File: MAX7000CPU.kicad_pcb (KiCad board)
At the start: 2 copper layers, 148.5 x 122 mm, 96 parts, among them J1 JTAG Conn_02x05_Odd_Even, J2 Instructions Conn_01x08_Male, J3 Module Input Conn_01x08_Male, J4 Module Output Conn_01x08_Male, J5 QPI Out Conn_01x08_Male, J6 QPI IN Conn_01x08_Male, J7 Conn_01x05_Male, J8 Barrel_Jack, SW1 Step SW_Push, SW2 CLK Mode SW_Push, SW3 Prog Select SW_DIP_x04, SW4 Reset SW_Push, U1 NE555P, U10 74LS573, U11 74LS241, U12 74LS241, U13 74LS573, U14 74LS573, U15 74LS573, U16 74LS573, U17 EPM7128slc84-15n, U18 LM2596S-5, U19 74LS241, U2 NE555P, U20 74LS241, U3 NE555P, U4 CLVC1GX04MDRLREP, U5 EPM7128slc84-15n, U6 74LS573, U7 SN74HC161N, U8 SN74HC161N, U9 IDT7132, Y1 Crystal

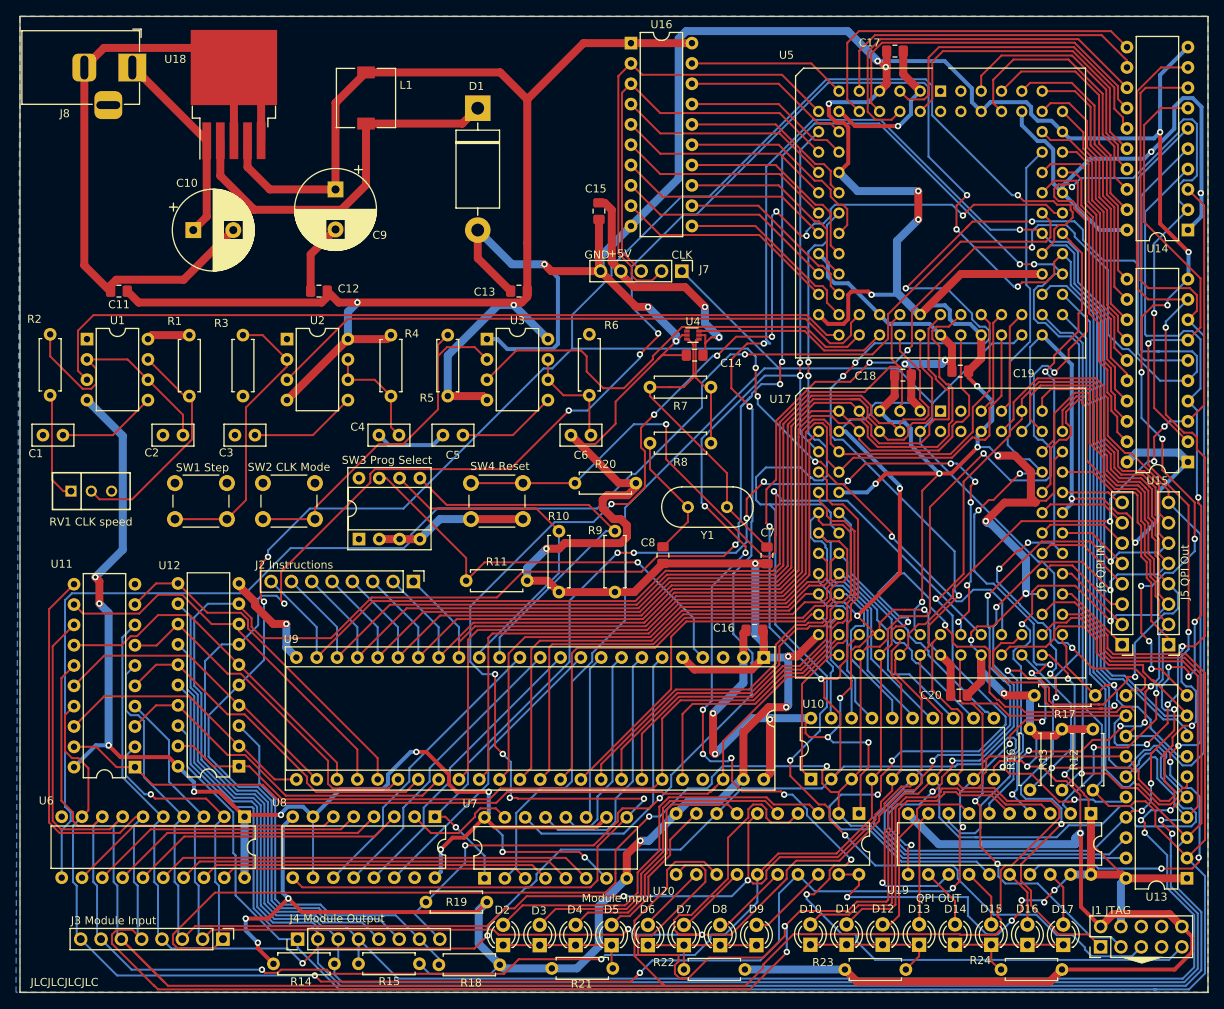
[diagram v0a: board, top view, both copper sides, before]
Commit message: auto routed
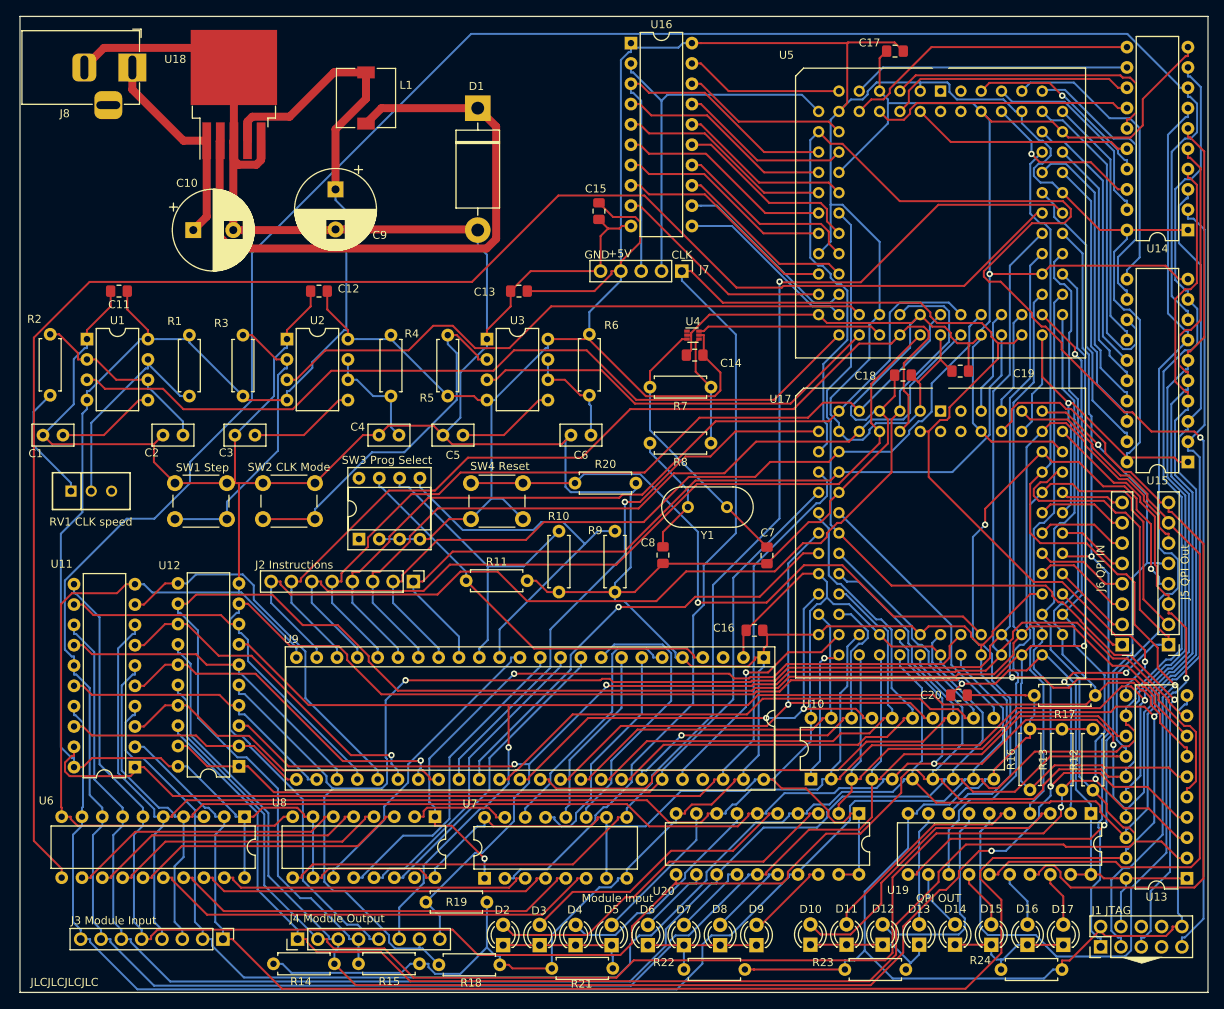
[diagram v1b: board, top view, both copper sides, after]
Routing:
- net /I4: track 464.4 -> 299.8 mm, vias 7 -> 0
- net /O6: track 370.5 -> 231.6 mm, vias 7 -> 2
- net /O7: track 322.3 -> 218.3 mm, vias 5 -> 2
- net /I5: track 394.1 -> 299.8 mm, vias 3 -> 0
- net /I6: track 339.7 -> 429.7 mm, vias 4 -> 0
- net /O5: track 313.3 -> 225.6 mm, vias 8 -> 1
- net /O4: track 334.5 -> 252.0 mm, vias 6 -> 1
- net /I3: track 361.6 -> 286.9 mm, vias 9 -> 1
- net /O2: track 310.4 -> 239.1 mm
- net /O1: track 300.1 -> 234.5 mm, vias 1 -> 3
- net /O0: track 295.9 -> 231.5 mm
- net /O3: track 302.4 -> 253.0 mm, vias 4 -> 0
- net JumpEnable: track 209.0 -> 159.9 mm, vias 11 -> 1
- net /I0: track 357.0 -> 314.8 mm, vias 7 -> 1
- net /Qo6: track 134.5 -> 96.4 mm, vias 3 -> 0
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- removed copper zone on F.Cu, net +5V
- removed copper zone on B.Cu, net GND
